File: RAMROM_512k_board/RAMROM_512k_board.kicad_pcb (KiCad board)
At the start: 2 copper layers, 100 x 100 mm, 46 parts, among them J1 BUS, J2 BUS, J3 BUS, J4 BUS, J6 STM32F411, J7 ., J8 ., J9 ., Q1 PMV450ENEAR, U1 SN74LVC245ANSR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

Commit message: Readme update
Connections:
- J6 pad 6: /uA9 -> /~{uMWR}
- J6 pad 9: /~{uMWR} -> /uA12
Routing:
- net /~{uMWR}: track 7.67 -> 5.50 mm
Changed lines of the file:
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@@
   (net 114 "unconnected-(U20-~{RCO}-Pad9)")
   (net 115 "/~{PLD}")
-  (net 116 "/uA9")
+  (net 116 "/uA12")
   (net 117 "/uA10")
   (net 118 "/uA11")
@@
       (net 106 "/CNT") (pinfunction "Pin_5") (pintype "passive"))
     (pad "6" thru_hole oval (at 0 12.7) (size 2.4 1.6) (drill 0.8) (layers "*.Cu" "*.Mask")
-      (net 116 "/uA9") (pinfunction "Pin_6") (pintype "passive"))
+      (net 119 "/~{uMWR}") (pinfunction "Pin_6") (pintype "passive"))
     (pad "7" thru_hole oval (at 0 15.24) (size 2.4 1.6) (drill 0.8) (layers "*.Cu" "*.Mask")
       (net 117 "/uA10") (pinfunction "Pin_7") (pintype "passive"))
@@
       (net 118 "/uA11") (pinfunction "Pin_8") (pintype "passive"))
     (pad "9" thru_hole oval (at 0 20.32) (size 2.4 1.6) (drill 0.8) (layers "*.Cu" "*.Mask")
-      (net 119 "/~{uMWR}") (pinfunction "Pin_9") (pintype "passive"))
+      (net 116 "/uA12") (pinfunction "Pin_9") (pintype "passive"))
     (pad "10" thru_hole oval (at 0 22.86) (size 2.4 1.6) (drill 0.8) (layers "*.Cu" "*.Mask")
       (net 120 "/~{uMRD}") (pinfunction "Pin_10") (pintype "passive"))
@@
   (segment (start 126.218806 92.944806) (end 127.141362 93.867362) (width 0.25) (layer "F.Cu") (net 115))
   (segment (start 109.22 83.947) (end 118.217806 92.944806) (width 0.25) (layer "F.Cu") (net 115))
-  (segment (start 113.665 99.187) (end 112.395 99.187) (width 0.25) (layer "F.Cu") (net 119))
-  (segment (start 112.395 99.187) (end 111.125 100.457) (width 0.25) (layer "F.Cu") (net 119))
-  (segment (start 111.125 102.362) (end 109.22 104.267) (width 0.25) (layer "F.Cu") (net 119))
-  (segment (start 111.125 100.457) (end 111.125 102.362) (width 0.25) (layer "F.Cu") (net 119))
+  (segment (start 112.7506 99.187) (end 110.2106 96.647) (width 0.25) (layer "F.Cu") (net 119))
+  (segment (start 110.2106 96.647) (end 109.22 96.647) (width 0.25) (layer "F.Cu") (net 119))
+  (segment (start 113.665 99.187) (end 112.7506 99.187) (width 0.25) (layer "F.Cu") (net 119))
   (segment (start 113.03 102.997) (end 113.665 102.997) (width 0.25) (layer "F.Cu") (net 120))
   (segment (start 109.22 106.807) (end 113.03 102.997) (width 0.25) (layer "F.Cu") (net 120))

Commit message: Readme update
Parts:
- added U3: 74LVC1G32, Package_TO_SOT_SMD:SOT-23-5_HandSoldering, F.Cu at (133.1, 68.7)
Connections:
- net /B10 renamed /TRST
- net /~{WP} renamed /WP
- U21 pad 11: Net-(U21-Pad1) -> unconnected-(U21-Pad11)
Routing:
- net /WP: track 49.8 -> 70.0 mm, vias 2 -> 3
- net GND: track 635.1 -> 642.1 mm
- net /~{MWR}: track 49.5 -> 54.0 mm, vias 2 -> 3
- net +3V3: track 525.8 -> 529.3 mm, vias 18 -> 19
- net Net-(U21-Pad1): track 6.57 -> 4.65 mm, vias 2 -> 0
- net /~{DATOE}: track 71.3 -> 70.3 mm

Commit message: python work
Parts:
- removed BT1: Battery_Cell, Battery:BatteryHolder_Keystone_103_1x20mm
- removed D2: BAT54C, Package_TO_SOT_SMD:SOT-23
- J6: value STM32F411 -> STM32F401
- U3: moved to B.Cu
- moved C9 18.9 mm to (184.1, 112.0), turned to 90 degrees
- moved U3 16.5 mm to (149.3, 65.8), turned to 180 degrees
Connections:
- C4 pad 1: Net-(C4-Pad1) -> +3V3
- J6 pad 7: /uA10 -> /~{RAMCSOR}
- U1 pad 19: Net-(U1-CE) -> /~{CSRAM}
- U21 pad 1: Net-(U21-Pad1) -> /~{DATOE}
- U21 pad 10: /~{MRD} -> /~{RAMCSOR}
- U21 pad 12: /~{MWR} -> unconnected-(U21-Pad12)
- U21 pad 13: /WP -> unconnected-(U21-Pad13)
- U21 pad 2: /~{RAMWE15} -> /~{MRD}
- U21 pad 3: Net-(U4-~{WE}) -> Net-(U4-~{OE})
- U21 pad 4: /~{DATOE} -> Net-(U21-Pad4)
- U21 pad 5: /~{MRD} -> /~{RAMWE15}
- U21 pad 6: Net-(U4-~{OE}) -> Net-(U4-~{WE})
- U21 pad 8: Net-(U1-CE) -> Net-(U4-~{CE})
- U21 pad 9: /~{MWR} -> /~{CSRAM}
- U3 pad 4: Net-(U21-Pad1) -> Net-(U21-Pad4)
- U4 pad 11: Net-(C4-Pad1) -> +3V3
- U4 pad 33: Net-(C4-Pad1) -> +3V3
- U4 pad 8: /~{CSRAM} -> Net-(U4-~{CE})
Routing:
- net /~{RAMCSOR}: track 0.00 -> 67.3 mm, vias 0 -> 3
- net Net-(U4-~{CE}): track 0.00 -> 50.2 mm, vias 0 -> 5
- net GND: track 642.1 -> 608.2 mm, vias 19 -> 20
- net Net-(C4-Pad1): track 32.6 -> 0.00 mm, vias 2 -> 0
- net /~{MWR}: track 54.0 -> 22.4 mm, vias 3 -> 2
- net /WP: track 70.0 -> 42.0 mm, vias 3 -> 1
- net /~{CSRAM}: track 23.0 -> 38.6 mm
- net Net-(U1-CE): track 6.70 -> 0.00 mm
- net Net-(U21-Pad4): track 0.00 -> 6.28 mm, vias 0 -> 1
- net /~{RAMWE15}: track 101.1 -> 107.2 mm
- net +3V3: track 529.3 -> 534.7 mm, vias 19 -> 21
- net Net-(U21-Pad1): track 4.65 -> 0.00 mm
- net /~{DATOE}: track 70.3 -> 65.9 mm
- net Net-(BT1-+): track 3.87 -> 0.00 mm
- net /~{MRD}: track 21.7 -> 23.7 mm
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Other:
- board text added: "*Unicomp v2* MOS 128k RAMROM Board v1.1"
- board text removed: "*Unicomp v2* MOS 128k RAMROM Board v1"

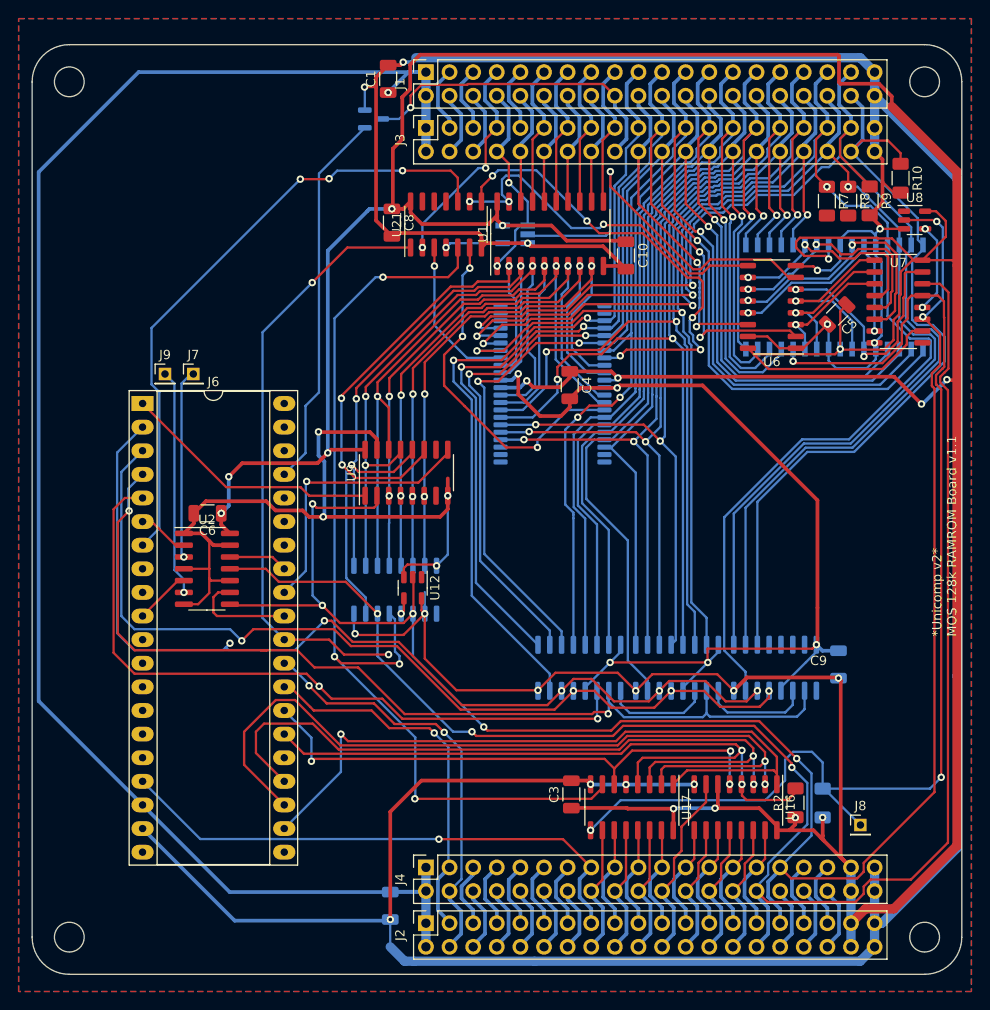
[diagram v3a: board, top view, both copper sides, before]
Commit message: SYM1 & KIM1 work, RAM Board update
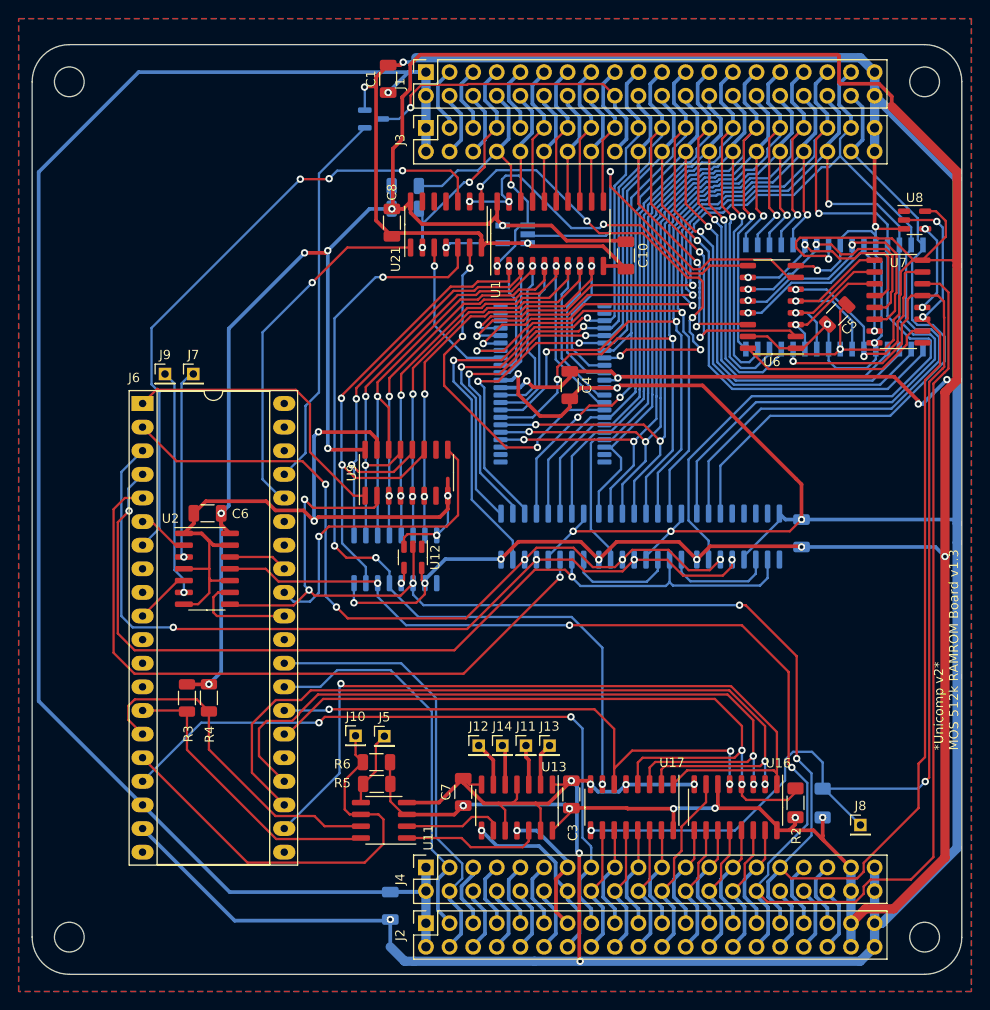
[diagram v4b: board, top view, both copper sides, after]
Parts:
- removed R10, R9: 10k, Resistor_SMD:R_1206_3216Metric_Pad1.30x1.75mm_HandSolder
- added C7: 100n, Capacitor_SMD:C_1206_3216Metric, F.Cu at (143.7, 125.7)
- added J10: ., Connector_PinHeader_2.00mm:PinHeader_1x01_P2.00mm_Vertical, F.Cu at (132.1, 119.7)
- added J11: ., Connector_PinHeader_2.00mm:PinHeader_1x01_P2.00mm_Vertical, F.Cu at (150.5, 120.7)
- added J12: ., Connector_PinHeader_2.00mm:PinHeader_1x01_P2.00mm_Vertical, F.Cu at (145.4, 120.7)
- added J13: ., Connector_PinHeader_2.00mm:PinHeader_1x01_P2.00mm_Vertical, F.Cu at (153.0, 120.7)
- added J14: ., Connector_PinHeader_2.00mm:PinHeader_1x01_P2.00mm_Vertical, F.Cu at (147.9, 120.7)
- added J5: ., Connector_PinHeader_2.00mm:PinHeader_1x01_P2.00mm_Vertical, F.Cu at (135.2, 119.7)
- added R3: 3k3, Resistor_SMD:R_1206_3216Metric, F.Cu at (114.0, 115.6)
- added R4: 3k3, Resistor_SMD:R_1206_3216Metric, F.Cu at (116.4, 115.6)
- added R5: 3k3, Resistor_SMD:R_1206_3216Metric, F.Cu at (134.4, 124.9)
- added R6: 3k3, Resistor_SMD:R_1206_3216Metric, F.Cu at (134.4, 122.5)
- added U11: DS1085, Package_SO:SOIC-8_3.9x4.9mm_P1.27mm, F.Cu at (135.2, 128.8)
- added U13: 74LVC125, Package_SO:SOIC-14_3.9x8.7mm_P1.27mm, F.Cu at (149.5, 127.4)
- R7, R8: footprint Resistor_SMD:R_1206_3216Metric_Pad1.30x1.75mm_HandSolder -> Resistor_SMD:R_1206_3216Metric; moved to B.Cu
- moved R8 47.6 mm to (137.5, 63.0), turned to 0 degrees
- moved R7 45.4 mm to (137.5, 60.6), turned to 0 degrees
- moved U18 14.7 mm to (152.2, 98.3)
- moved U19 14.7 mm to (162.7, 98.3)
- moved U20 14.7 mm to (173.3, 98.3)
- moved C9 14.7 mm to (180.1, 97.9)
- moved U12 3.28 mm to (138.3, 100.5)
- moved U10 3.28 mm to (136.4, 100.7)
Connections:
- J6 pad 14: /B6 -> /SCL
- J6 pad 15: /B7 -> /SDA
- J6 pad 16: /B8 -> /CTRL1
- J6 pad 30: /~{DATOE} -> /A4
- J6 pad 36: /B2 -> /~{DATOE}
- R7 pad 1: /A16 -> +3V3
- R7 pad 2: GND -> /~{MWR}
- R8 pad 1: /A17 -> +3V3
- R8 pad 2: GND -> /~{MRD}
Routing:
- net +3V3: track 534.7 -> 587.0 mm, vias 21 -> 26
- net /CTRL1: track 0.00 -> 47.7 mm
- net /SDA: track 0.00 -> 37.0 mm
- net /SCL: track 0.00 -> 31.3 mm
- net /~{DATOE}: track 65.9 -> 38.7 mm, vias 2 -> 1
- net GND: track 608.2 -> 627.7 mm, vias 20 -> 23
- net /~{CNTOE}: track 103.3 -> 83.9 mm
- net /~{RAMWE15}: track 107.2 -> 90.7 mm
- net /A0: track 87.7 -> 71.4 mm
- net /A3: track 128.3 -> 112.0 mm
- net /A8: track 110.2 -> 94.0 mm
- net /A19: track 85.0 -> 69.1 mm
- net /A2: track 117.9 -> 102.1 mm
- net /A1: track 105.8 -> 90.0 mm
- net /A18: track 141.5 -> 125.8 mm
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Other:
- board text added: "*Unicomp v2* MOS 512k RAMROM Board v1.3"
- board text removed: "*Unicomp v2* MOS 128k RAMROM Board v1.1"
- board text removed: "C9"
- board text removed: "U18"

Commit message: SYM1 & KIM1 work, RAM Board update
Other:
- board text added: "*Unicomp v2* 512k SRAM Board v1.3"
- board text removed: "*Unicomp v2* MOS 512k RAMROM Board v1.3"
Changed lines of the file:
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@@
   (gr_line (start 193.34 145.346005) (end 101.34 145.346005)
     (stroke (width 0.1) (type solid)) (layer "Edge.Cuts"))
-  (gr_text "*Unicomp v2*\nMOS 512k RAMROM Board v1.3" (at 195.6816 121.2596 90) (layer "F.SilkS")
+  (gr_text "*Unicomp v2*\n512k SRAM Board v1.3" (at 195.6816 121.2596 90) (layer "F.SilkS")
     (effects (font (size 1 1) (thickness 0.15)) (justify left))
   )

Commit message: Documentation update
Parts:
- removed J7, J9: ., Connector_PinHeader_2.00mm:PinHeader_1x01_P2.00mm_Vertical
- added C11: 100n, Capacitor_SMD:C_1206_3216Metric, B.Cu at (130.0, 101.0)
- C6: moved to B.Cu
- moved C6 73.7 mm to (186.1, 119.1), turned to -90 degrees
- moved U2 71.8 mm to (186.0, 118.4)
- moved R1 19.5 mm to (162.9, 127.5), turned to 180 degrees
- moved J8 5.32 mm to (191.3, 131.4)
- moved U12 3.18 mm to (140.9, 102.4), turned to 180 degrees
- moved R4 0.57 mm to (116.4, 116.2)
- moved R3 0.56 mm to (114.0, 116.2)
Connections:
- net /UMISO renamed /uMISO
- J6 pad 30: /A4 -> /uA4
- U10 pad 11: /SCK -> /uSCK
- U10 pad 14: /MOSI -> /uMOSI
- U12 pad 2: /SCK -> /uSCK
- U2 pad 2: /~{uMWR} -> /uSCK
- U2 pad 3: Net-(J7-Pin_1) -> /SCK
- U2 pad 5: /~{uMRD} -> /uSCK
- U2 pad 6: Net-(J9-Pin_1) -> /SCK
- U2 pad 8: /SCK -> /MOSI
- U2 pad 9: /uSCK -> /uMOSI
- U7 pad 11: /SCK -> /uSCK
- U7 pad 14: /MOSI -> /uMOSI
- U8 pad 2: /SCK -> /uSCK
- U9 pad 2: /SCK -> /uSCK
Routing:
- net /SCK: track 209.6 -> 29.4 mm, vias 7 -> 0
- net /uSCK: track 11.4 -> 181.9 mm, vias 0 -> 6
- net /MOSI: track 184.6 -> 35.2 mm, vias 3 -> 0
- net /uMOSI: track 6.37 -> 143.8 mm, vias 0 -> 4
- net Net-(J9-Pin_1): track 24.3 -> 0.00 mm, vias 1 -> 0
- net +3V3: track 587.0 -> 608.8 mm
- net Net-(J7-Pin_1): track 20.2 -> 0.00 mm, vias 1 -> 0
- net /~{uMRD}: track 5.39 -> 0.00 mm
- net /~{uMWR}: track 4.51 -> 0.00 mm
- net GND: track 627.7 -> 631.2 mm, vias 23 -> 28
- net /CD0: track 68.9 -> 72.0 mm
- net /uMISO: track 34.0 -> 36.9 mm, vias 1 -> 0
- net Net-(U10-RCLK): track 1.77 -> 3.95 mm
- net /~{RAMWE15}: track 90.7 -> 91.9 mm
- net /CD1: track 60.6 -> 61.2 mm
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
